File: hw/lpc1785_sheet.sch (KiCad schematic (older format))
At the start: 25 parts, among them J2 ARM_JTAG_SWD_HEADER_10_PINSMD, J3 HEADER_USART_2_SMD, U4 LPC1785FBD208_551QFP50, X1 XTAL_7A-20.000MAAJ-T

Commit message: multiple bug fixes, uv terminal SDO interface
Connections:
- wire segments 181 -> 234
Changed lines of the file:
@@
 	5500 4100 5600 4100
 Wire Wire Line
-	5500 3800 5500 4300
-Wire Wire Line
-	4700 4000 5600 4000
+	5500 3800 5500 3900
+Wire Wire Line
+	5500 3900 5500 4000
+Wire Wire Line
+	5500 4000 5500 4100
+Wire Wire Line
+	5500 4100 5500 4300
+Wire Wire Line
+	4700 4000 4850 4000
+Wire Wire Line
+	4850 4000 5000 4000
+Wire Wire Line
+	5000 4000 5150 4000
+Wire Wire Line
+	5150 4000 5500 4000
+Wire Wire Line
+	5500 4000 5600 4000
 Wire Wire Line
 	5600 3900 5500 3900
@@
 $EndComp
 Wire Wire Line
-	5400 5300 5400 5550
+	5400 5300 5400 5400
+Wire Wire Line
+	5400 5400 5400 5500
+Wire Wire Line
+	5400 5500 5400 5550
 Wire Wire Line
 	5400 5300 5600 5300
@@
 	4150 4250 4150 4350
 Wire Wire Line
-	4050 4350 4350 4350
+	4050 4350 4150 4350
+Wire Wire Line
+	4150 4350 4250 4350
+Wire Wire Line
+	4250 4350 4350 4350
 Connection ~ 4250 4350
 Wire Wire Line
@@
 Connection ~ 4150 4350
 Wire Wire Line
-	3900 4750 5250 4750
+	3900 4750 4150 4750
+Wire Wire Line
+	4150 4750 5250 4750
 Wire Wire Line
 	4150 4750 4150 4650
@@
 Connection ~ 4150 4750
 Wire Wire Line
-	3900 4950 4550 4950
-Wire Wire Line
-	4350 4650 4350 10600
+	3900 4950 4250 4950
+Wire Wire Line
+	4250 4950 4550 4950
+Wire Wire Line
+	4350 4650 4350 5450
+Wire Wire Line
+	4350 5450 4350 10600
 Connection ~ 4350 5450
 Wire Wire Line
@@
 $EndComp
 Wire Wire Line
-	4050 4850 4050 5550
+	4050 4850 4050 5050
+Wire Wire Line
+	4050 5050 4050 5550
 Wire Wire Line
 	4050 4850 3900 4850
@@
 Text Label 4550 4950 0    60   ~ 0
 SWDCLK
-Wire Wire Line
-	4350 10600 5050 10600
 Wire Wire Line
 	4350 5450 3900 5450
@@
 Connection ~ 11000 3850
 Wire Wire Line
-	10850 3850 11300 3850
+	10850 3850 11000 3850
+Wire Wire Line
+	11000 3850 11150 3850
+Wire Wire Line
+	11150 3850 11300 3850
 $Comp
 L 100nF C24
@@
 $EndComp
 Wire Wire Line
-	10850 4150 11900 4150
+	10850 4150 11000 4150
+Wire Wire Line
+	11000 4150 11150 4150
+Wire Wire Line
+	11150 4150 11800 4150
+Wire Wire Line
+	11800 4150 11900 4150
 Connection ~ 11000 4150
 Connection ~ 11150 4150
@@
 	11900 4050 11800 4050
 Wire Wire Line
-	11800 4050 11800 4350
+	11800 4050 11800 4150
+Wire Wire Line
+	11800 4150 11800 4250
+Wire Wire Line
+	11800 4250 11800 4350
 Connection ~ 11800 4150
 Wire Wire Line
@@
 Connection ~ 11800 4250
 Wire Wire Line
-	11300 3750 11900 3750
+	11300 3750 11800 3750
+Wire Wire Line
+	11800 3750 11900 3750
 Wire Wire Line
 	11300 3850 11300 3750
@@
 	11900 3650 11800 3650
 Wire Wire Line
-	11800 3550 11800 3750
+	11800 3550 11800 3650
+Wire Wire Line
+	11800 3650 11800 3750
 Connection ~ 11800 3750
 Wire Wire Line
@@
 $EndComp
 Wire Wire Line
-	4400 9700 5050 9700
+	4400 9700 4550 9700
+Wire Wire Line
+	4550 9700 4700 9700
+Wire Wire Line
+	4700 9700 4850 9700
+Wire Wire Line
+	4850 9700 4950 9700
+Wire Wire Line
+	4950 9700 5050 9700
 Connection ~ 4550 9700
 Connection ~ 4700 9700
 Connection ~ 4850 9700
 Wire Wire Line
-	4950 9700 4950 10000
+	4950 9700 4950 9800
+Wire Wire Line
+	4950 9800 4950 9900
+Wire Wire Line
+	4950 9900 4950 10000
 Wire Wire Line
 	4950 9800 5050 9800
@@
 Connection ~ 4950 9900
 Wire Wire Line
-	4400 9400 5050 9400
+	4400 9400 4550 9400
+Wire Wire Line
+	4550 9400 4700 9400
+Wire Wire Line
+	4700 9400 4850 9400
+Wire Wire Line
+	4850 9400 4950 9400
+Wire Wire Line
+	4950 9400 5050 9400
 Connection ~ 4850 9400
 Connection ~ 4700 9400
 Connection ~ 4550 9400
 Wire Wire Line
-	4950 9100 4950 9400
+	4950 9100 4950 9200
+Wire Wire Line
+	4950 9200 4950 9300
+Wire Wire Line
+	4950 9300 4950 9400
 Connection ~ 4950 9400
 Wire Wire Line
@@
 $EndComp
 Wire Wire Line
-	10750 8900 11800 8900
+	10750 8900 10900 8900
+Wire Wire Line
+	10900 8900 11050 8900
+Wire Wire Line
+	11050 8900 11700 8900
+Wire Wire Line
+	11700 8900 11800 8900
 Connection ~ 10900 8900
 Connection ~ 11050 8900
 Wire Wire Line
-	11700 8900 11700 9100
+	11700 8900 11700 9000
+Wire Wire Line
+	11700 9000 11700 9100
 Wire Wire Line
 	11700 9000 11800 9000
@@
 	10750 9250 10750 9200
 Wire Wire Line
-	10750 9200 11050 9200
+	10750 9200 10900 9200
+Wire Wire Line
+	10900 9200 11050 9200
 Connection ~ 10900 9200
 $Comp
@@
 $EndComp
 Wire Wire Line
-	11500 9500 11750 9500
+	11500 9500 11600 9500
+Wire Wire Line
+	11600 9500 11750 9500
 Wire Wire Line
 	11750 9500 11750 9400
@@
 	11750 9300 11750 9200
 Wire Wire Line
-	11750 9200 11500 9200
+	11750 9200 11600 9200
+Wire Wire Line
+	11600 9200 11500 9200
 $Comp
 L 18pF C30
@@
 Connection ~ 11600 9200
 Wire Wire Line
-	11200 9200 11200 9500
+	11200 9200 11200 9300
+Wire Wire Line
+	11200 9300 11200 9500
 $Comp
 L GND #PWR034
@@
 	11800 9600 11700 9600
 Wire Wire Line
-	11700 9600 11700 9850
+	11700 9600 11700 9700
+Wire Wire Line
+	11700 9700 11700 9800
+Wire Wire Line
+	11700 9800 11700 9850
 Wire Wire Line
 	11700 9700 11800 9700
@@
 	15800 9000 15900 9000
 Wire Wire Line
-	15800 10400 18450 10400
+	15800 10400 17000 10400
+Wire Wire Line
+	17000 10400 18350 10400
+Wire Wire Line
+	18350 10400 18450 10400
 Wire Wire Line
 	15800 10600 16700 10600
@@
 	16700 10600 16700 10300
 Wire Wire Line
-	16700 10300 18450 10300
+	16700 10300 17000 10300
+Wire Wire Line
+	17000 10300 18350 10300
+Wire Wire Line
+	18350 10300 18450 10300
 Wire Wire Line
 	18450 10200 18350 10200
@@
 $EndComp
 Wire Wire Line
-	18250 10800 18250 11000
+	18250 10800 18250 10900
+Wire Wire Line
+	18250 10900 18250 11000
 Wire Wire Line
 	18250 10800 18450 10800
@@
 	4400 9850 4400 9700
 Wire Wire Line
-	4700 4300 5150 4300
+	4700 4300 4850 4300
+Wire Wire Line
+	4850 4300 5000 4300
+Wire Wire Line
+	5000 4300 5150 4300
 Wire Wire Line
 	15900 11200 15800 11200
@@
 Wire Wire Line
 	9450 4000 8700 4000
+Wire Wire Line
+	4350 10600 5050 10600
 $EndSCHEMATC

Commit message: starting to design hw 5.0, with variable current source for LCD backlight
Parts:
- removed D4: WL-SMCW-150060BS75000-B, wurth_LEDS:Wuerth_Elektronik_LEDs_rev15b-0603, symbol WL-SMCW-150060BS75000-B
- removed J3: HEADER_USART_2_SMD, usevolt:HEADER_4_2_SMD, symbol HEADER_USART_2_SMD
- removed R8: 470, multicomp:Multicomp-RESC1608X60N, symbol 470
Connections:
- net labels removed: RXD, TXD
- wire segments 234 -> 162

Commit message: still implementing treeview, not ready
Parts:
- added R301: 10K, multicomp:0603, symbol 10K
- U4: symbol LPC1785FBD208_551QFP50 -> LPC1785FBD208_551QFP50-RESCUE-display
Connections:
- net labels removed: VDD_SENSE
- wire segments 162 -> 163
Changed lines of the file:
@@
 $EndDescr
 $Comp
-L LPC1785FBD208_551QFP50 U4
+L LPC1785FBD208_551QFP50-RESCUE-display U4
 U 1 1 57B485E7
 P 6700 5400
+AR Path="/57B485E7" Ref="U4"  Part="1"
+AR Path="/57B4853E/57B485E7" Ref="U4"  Part="1"
 F 0 "U4" H 7150 7354 45  0000 C CNN
 F 1 "LPC1785FBD208_551QFP50" H 7150 7270 45  0000 C CNN
@@
 $EndComp
 $Comp
-L LPC1785FBD208_551QFP50 U4
+L LPC1785FBD208_551QFP50-RESCUE-display U4
 U 2 1 57B48643
 P 13000 5050
+AR Path="/57B48643" Ref="U4"  Part="2"
+AR Path="/57B4853E/57B48643" Ref="U4"  Part="2"
 F 0 "U4" H 14150 6804 45  0000 C CNN
 F 1 "LPC1785FBD208_551QFP50" H 14150 6720 45  0000 C CNN
@@
 $EndComp
 $Comp
-L LPC1785FBD208_551QFP50 U4
+L LPC1785FBD208_551QFP50-RESCUE-display U4
 U 3 1 57B486B3
 P 5950 10500
+AR Path="/57B486B3" Ref="U4"  Part="3"
+AR Path="/57B4853E/57B486B3" Ref="U4"  Part="3"
 F 0 "U4" H 7050 12154 45  0000 C CNN
 F 1 "LPC1785FBD208_551QFP50" H 7050 12070 45  0000 C CNN
@@
 $EndComp
 $Comp
-L LPC1785FBD208_551QFP50 U4
+L LPC1785FBD208_551QFP50-RESCUE-display U4
 U 4 1 57B4870D
 P 12800 10600
+AR Path="/57B4870D" Ref="U4"  Part="4"
+AR Path="/57B4853E/57B4870D" Ref="U4"  Part="4"
 F 0 "U4" H 13800 12554 45  0000 C CNN
 F 1 "LPC1785FBD208_551QFP50" H 13800 12470 45  0000 C CNN
@@
 Wire Wire Line
 	9150 9100 9050 9100
-Text HLabel 9150 9800 2    60   Input ~ 0
+Text HLabel 10000 9800 2    60   Input ~ 0
 LCD_DE
 Text HLabel 9150 9900 2    60   Input ~ 0
@@
 	9050 9900 9150 9900
 Wire Wire Line
-	9150 9800 9050 9800
+	9050 9800 10000 9800
 Text HLabel 9150 10800 2    60   Input ~ 0
 EMC_A7
@@
 Connection ~ 11700 9000
 $Comp
-L GND #PWR309
+L GND #PWR310
 U 1 1 57B6EDB0
 P 10750 9250
-F 0 "#PWR309" H 10750 9000 50  0001 C CNN
+F 0 "#PWR310" H 10750 9000 50  0001 C CNN
 F 1 "GND" H 10755 9077 50  0000 C CNN
 F 2 "" H 10750 9250 50  0000 C CNN
@@
 	11800 9300 11750 9300
 Wire Wire Line
-	11750 9300 11750 9200
-Wire Wire Line
-	11750 9200 11500 9200
+	11750 9200 11750 9300
+Wire Wire Line
+	11500 9200 11750 9200
 $Comp
 L 18pF C30
@@
 	11200 9200 11200 9500
 $Comp
-L GND #PWR312
+L GND #PWR313
 U 1 1 57B6F87A
 P 11100 9400
-F 0 "#PWR312" H 11100 9150 50  0001 C CNN
+F 0 "#PWR313" H 11100 9150 50  0001 C CNN
 F 1 "GND" H 11105 9227 50  0000 C CNN
 F 2 "" H 11100 9400 50  0000 C CNN
@@
 Connection ~ 11700 9700
 $Comp
-L GND #PWR313
+L GND #PWR314
 U 1 1 57B7073F
 P 11700 9850
-F 0 "#PWR313" H 11700 9600 50  0001 C CNN
+F 0 "#PWR314" H 11700 9600 50  0001 C CNN
 F 1 "GND" H 11705 9677 50  0000 C CNN
 F 2 "" H 11700 9850 50  0000 C CNN
@@
 Wire Wire Line
 	11700 10400 11800 10400
-Text HLabel 11700 10700 0    60   Input ~ 0
+Text HLabel 5500 7300 0    60   Input ~ 0
 LCD_BACKLIGHT
 Wire Wire Line
-	11700 10700 11800 10700
-Text HLabel 15900 11200 2    60   Input ~ 0
+	5500 7300 5600 7300
+Text HLabel 5500 7200 0    60   Input ~ 0
 BUZZER
 Text HLabel 15900 12100 2    60   Input ~ 0
@@
 Wire Wire Line
 	8700 5300 8800 5300
-Wire Wire Line
-	8800 5100 8700 5100
-Text HLabel 8800 5100 2    60   Input ~ 0
-VDD_SENSE
 $Bitmap
 Pos 22650 15250
@@
 SPI_RESET
 $Comp
-L +3V3 #PWR308
+L +3V3 #PWR309
 U 1 1 57BCA081
 P 10750 8800
-F 0 "#PWR308" H 10750 8650 50  0001 C CNN
+F 0 "#PWR309" H 10750 8650 50  0001 C CNN
 F 1 "+3V3" H 10765 8973 50  0000 C CNN
 F 2 "" H 10750 8800 50  0000 C CNN
@@
 	4400 9250 4400 9400
 $Comp
-L +3V3 #PWR310
+L +3V3 #PWR311
 U 1 1 57BCB2A0
 P 10850 3700
-F 0 "#PWR310" H 10850 3550 50  0001 C CNN
+F 0 "#PWR311" H 10850 3550 50  0001 C CNN
 F 1 "+3V3" H 10865 3873 50  0000 C CNN
 F 2 "" H 10850 3700 50  0000 C CNN
@@
 	10850 3700 10850 3850
 $Comp
-L GND #PWR311
+L GND #PWR312
 U 1 1 57BCB9E7
 P 10850 4300
-F 0 "#PWR311" H 10850 4050 50  0001 C CNN
+F 0 "#PWR312" H 10850 4050 50  0001 C CNN
 F 1 "GND" H 10855 4127 50  0000 C CNN
 F 2 "" H 10850 4300 50  0000 C CNN
@@
 	4700 4300 5150 4300
 Wire Wire Line
-	15900 11200 15800 11200
+	5500 7200 5600 7200
 Wire Wire Line
 	4350 10600 5050 10600
+$Comp
+L 10K R301
+U 1 1 58F5514D
+P 9800 9950
+F 0 "R301" V 9808 10008 45  0000 L CNN
+F 1 "10K" V 9892 10008 45  0000 L CNN
+F 2 "multicomp:0603" H 9830 10100 20  0001 C CNN
+F 3 "http://www.farnell.com/datasheets/1788326.pdf?_ga=1.214208087.1948984246.1460023966" H 9769 9989 60  0001 C CNN
+F 4 "9330399" H 10169 10389 60  0001 C CNN "1st Source Part Number"
+F 5 "Farnell" H 10069 10289 60  0001 C CNN "1st Source"
+F 6 "MC0063W0603110K" H 9969 10189 60  0001 C CNN "Manufacturer Part Number"
+F 7 "MULTICOMP" H 9869 10089 60  0001 C CNN "Manufacturer"
+	1    9800 9950
+	0    1    1    0
+$EndComp
+$Comp
+L GND #PWR308
+U 1 1 58F551E0
+P 9800 10200
+F 0 "#PWR308" H 9800 9950 50  0001 C CNN
+F 1 "GND" H 9805 10027 50  0000 C CNN
+F 2 "" H 9800 10200 50  0000 C CNN
+F 3 "" H 9800 10200 50  0000 C CNN
+	1    9800 10200
+	1    0    0    -1
+$EndComp
+Wire Wire Line
+	9800 10200 9800 10150
+Wire Wire Line
+	9800 9850 9800 9800
+Connection ~ 9800 9800
 $EndSCHEMATC

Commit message: version control bug: pwr_supply_sheet now has fuse for LCD as in hw 1.5.0
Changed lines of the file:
@@
 	11800 9300 11750 9300
 Wire Wire Line
-	11750 9200 11750 9300
+	11750 9300 11750 9200
 Wire Wire Line
-	11500 9200 11750 9200
+	11750 9200 11500 9200
 $Comp
 L 18pF C30

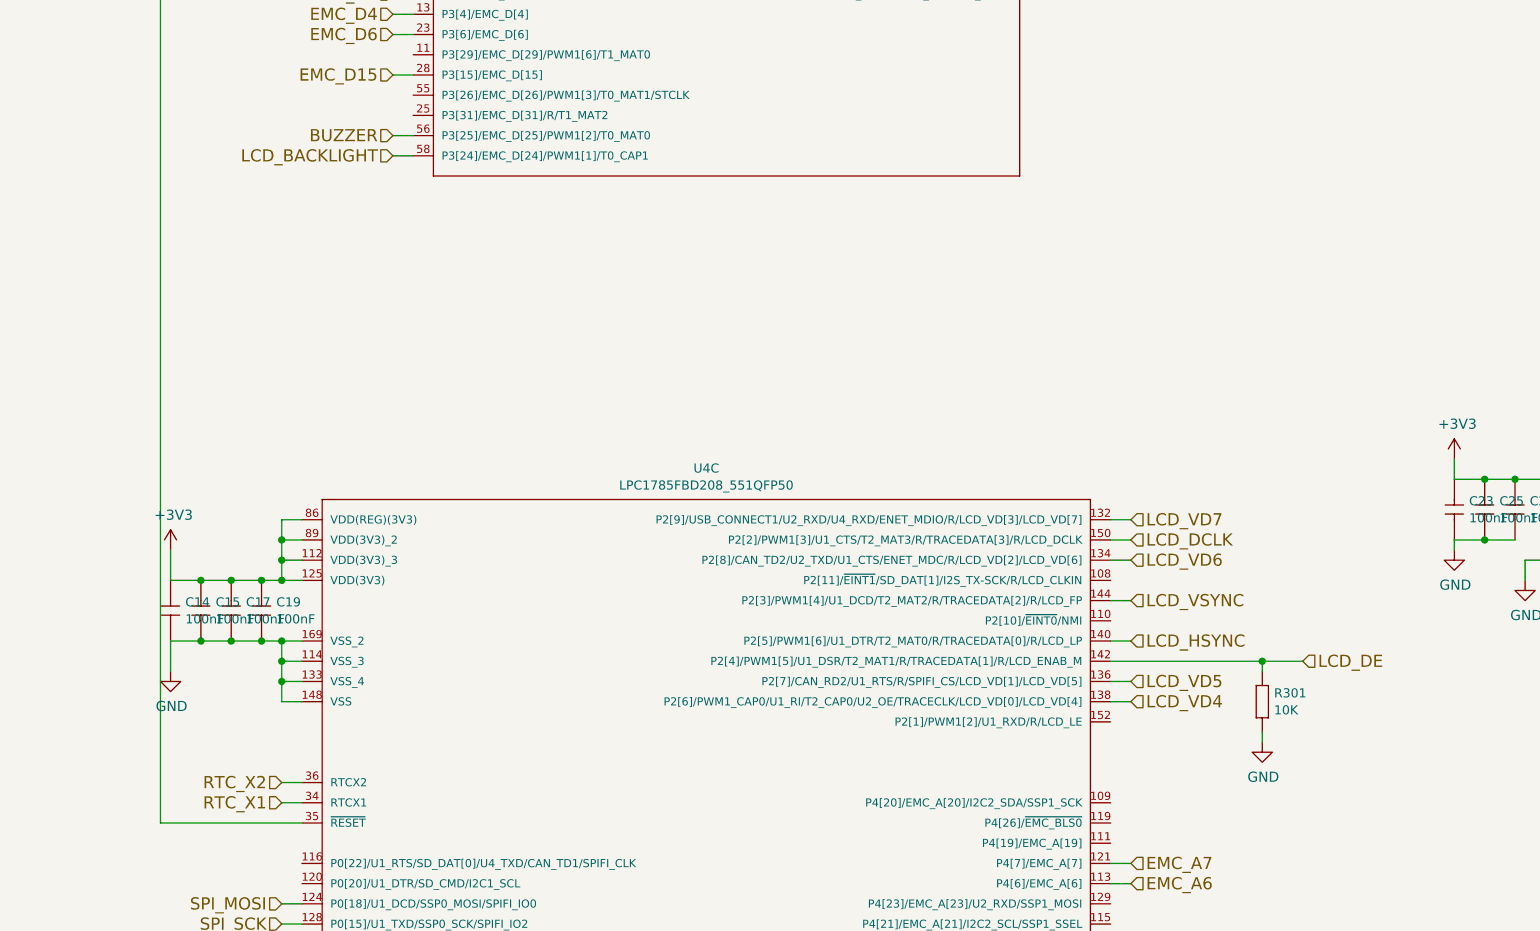
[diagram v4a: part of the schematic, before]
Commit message: hw version 1.6.0
* LCD backlight remains off while booting
* BUZZER amplifying MOSFET circuit changed to low side driving
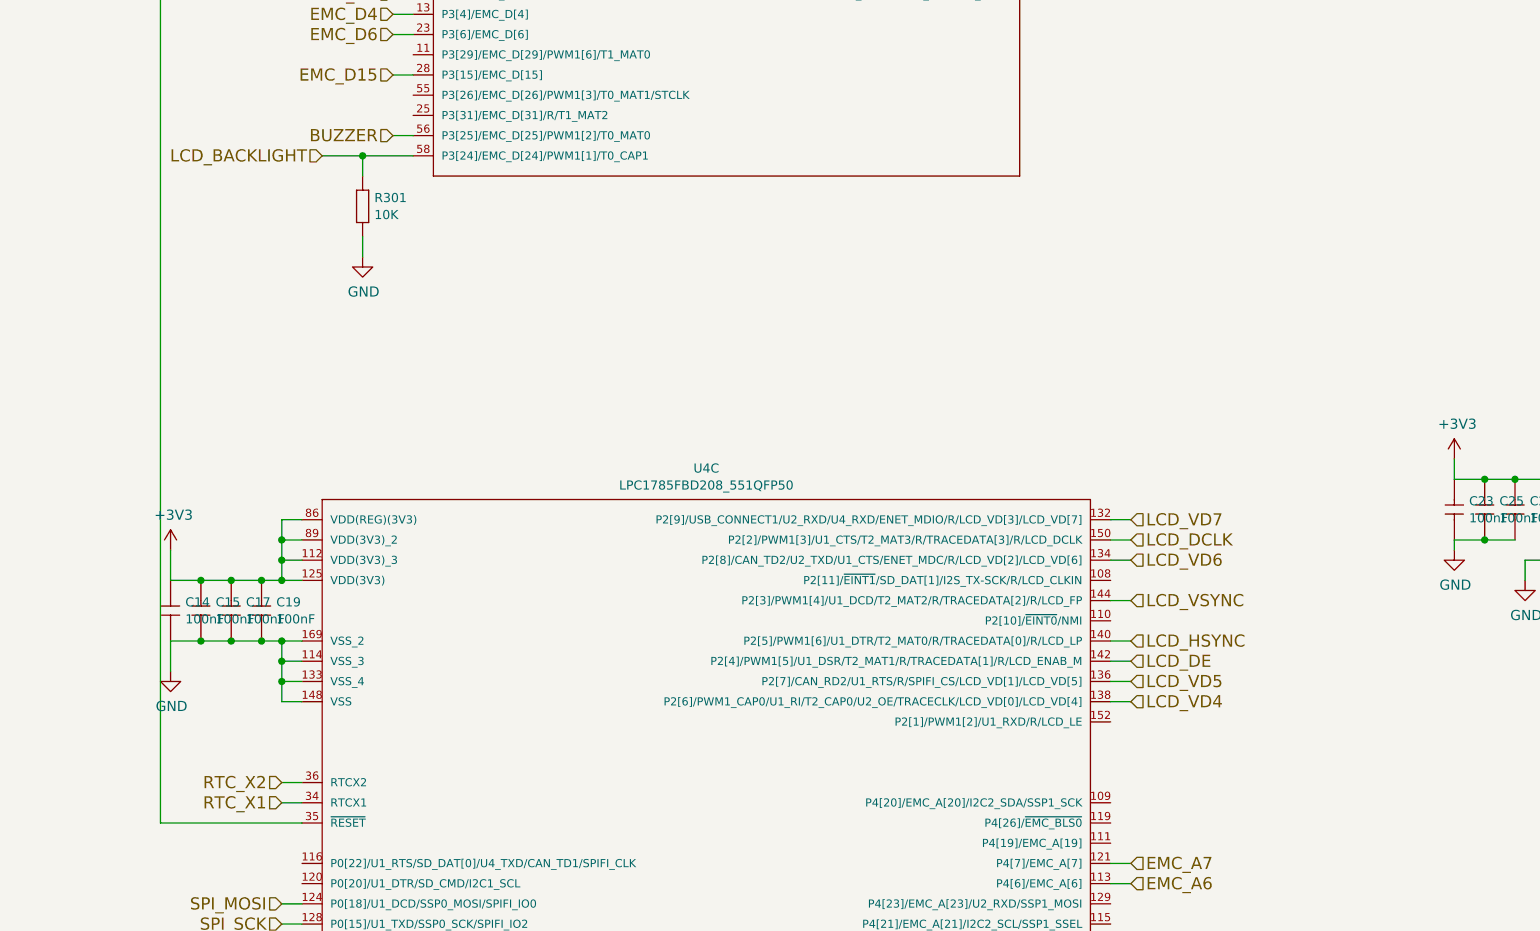
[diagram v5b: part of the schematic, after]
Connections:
- net LCD_BACKLIGHT: now also R301.2 (R2)
- net LCD_DE: no longer R301.2 (R2)
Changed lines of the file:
@@
 	4700 4400 4700 4300
 $Comp
-L GND #PWR307
+L GND #PWR308
 U 1 1 57B55D95
 P 5400 5550
-F 0 "#PWR307" H 5400 5300 50  0001 C CNN
+F 0 "#PWR308" H 5400 5300 50  0001 C CNN
 F 1 "GND" H 5405 5377 50  0000 C CNN
 F 2 "" H 5400 5550 50  0000 C CNN
@@
 Wire Wire Line
 	9150 9100 9050 9100
-Text HLabel 10000 9800 2    60   Input ~ 0
+Text HLabel 9150 9800 2    60   Input ~ 0
 LCD_DE
 Text HLabel 9150 9900 2    60   Input ~ 0
@@
 	9050 9900 9150 9900
 Wire Wire Line
-	9050 9800 10000 9800
+	9050 9800 9150 9800
 Text HLabel 9150 10800 2    60   Input ~ 0
 EMC_A7
@@
 Wire Wire Line
 	11700 10400 11800 10400
-Text HLabel 5500 7300 0    60   Input ~ 0
+Text HLabel 5150 7300 0    60   Input ~ 0
 LCD_BACKLIGHT
 Wire Wire Line
-	5500 7300 5600 7300
+	5150 7300 5600 7300
 Text HLabel 5500 7200 0    60   Input ~ 0
 BUZZER
@@
 Wire Wire Line
 	4350 10600 5050 10600
+Wire Wire Line
+	5350 7400 5350 7300
+Connection ~ 5350 7300
+$Comp
+L GND #PWR307
+U 1 1 59507EAE
+P 5350 7800
+F 0 "#PWR307" H 5350 7550 50  0001 C CNN
+F 1 "GND" H 5355 7627 50  0000 C CNN
+F 2 "" H 5350 7800 50  0000 C CNN
+F 3 "" H 5350 7800 50  0000 C CNN
+	1    5350 7800
+	1    0    0    -1
+$EndComp
+Wire Wire Line
+	5350 7800 5350 7700
 $Comp
 L 10K R301
-U 1 1 58F5514D
-P 9800 9950
-F 0 "R301" V 9808 10008 45  0000 L CNN
-F 1 "10K" V 9892 10008 45  0000 L CNN
-F 2 "multicomp:0603" H 9830 10100 20  0001 C CNN
-F 3 "http://www.farnell.com/datasheets/1788326.pdf?_ga=1.214208087.1948984246.1460023966" H 9769 9989 60  0001 C CNN
-F 4 "9330399" H 10169 10389 60  0001 C CNN "1st Source Part Number"
-F 5 "Farnell" H 10069 10289 60  0001 C CNN "1st Source"
-F 6 "MC0063W0603110K" H 9969 10189 60  0001 C CNN "Manufacturer Part Number"
-F 7 "MULTICOMP" H 9869 10089 60  0001 C CNN "Manufacturer"
-	1    9800 9950
-	0    1    1    0
-$EndComp
-$Comp
-L GND #PWR308
-U 1 1 58F551E0
-P 9800 10200
-F 0 "#PWR308" H 9800 9950 50  0001 C CNN
-F 1 "GND" H 9805 10027 50  0000 C CNN
-F 2 "" H 9800 10200 50  0000 C CNN
-F 3 "" H 9800 10200 50  0000 C CNN
-	1    9800 10200
-	1    0    0    -1
-$EndComp
-Wire Wire Line
-	9800 10200 9800 10150
-Wire Wire Line
-	9800 9850 9800 9800
-Connection ~ 9800 9800
+U 1 1 595084C8
+P 5350 7500
+F 0 "R301" V 5358 7558 45  0000 L CNN
+F 1 "10K" V 5442 7558 45  0000 L CNN
+F 2 "multicomp:0603" H 5380 7650 20  0001 C CNN
+F 3 "http://www.farnell.com/datasheets/1788326.pdf?_ga=1.214208087.1948984246.1460023966" H 5319 7539 60  0001 C CNN
+F 4 "9330399" H 5719 7939 60  0001 C CNN "1st Source Part Number"
+F 5 "Farnell" H 5619 7839 60  0001 C CNN "1st Source"
+F 6 "MC0063W0603110K" H 5519 7739 60  0001 C CNN "Manufacturer Part Number"
+F 7 "MULTICOMP" H 5419 7639 60  0001 C CNN "Manufacturer"
+	1    5350 7500
+	0    1    1    0
+$EndComp
 $EndSCHEMATC

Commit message: small modifications to schematic
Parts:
- removed R301: 10K, multicomp:0603, symbol 10K
- added R?: 1K, multicomp:0603, symbol 1K
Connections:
- net GND: now also R?.1 (R1)
- net LCD_BACKLIGHT: now also R?.2 (R2)
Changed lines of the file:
@@
 	5350 7800 5350 7700
 $Comp
-L 10K R301
-U 1 1 595084C8
+L 1K R?
+U 1 1 59515664
 P 5350 7500
-F 0 "R301" V 5358 7558 45  0000 L CNN
-F 1 "10K" V 5442 7558 45  0000 L CNN
+F 0 "R?" V 5358 7558 45  0000 L CNN
+F 1 "1K" V 5442 7558 45  0000 L CNN
 F 2 "multicomp:0603" H 5380 7650 20  0001 C CNN
-F 3 "http://www.farnell.com/datasheets/1788326.pdf?_ga=1.214208087.1948984246.1460023966" H 5319 7539 60  0001 C CNN
-F 4 "9330399" H 5719 7939 60  0001 C CNN "1st Source Part Number"
+F 3 "" H 5319 7539 60  0001 C CNN
+F 4 "9330380" H 5719 7939 60  0001 C CNN "1st Source Part Number"
 F 5 "Farnell" H 5619 7839 60  0001 C CNN "1st Source"
-F 6 "MC0063W0603110K" H 5519 7739 60  0001 C CNN "Manufacturer Part Number"
+F 6 "MC0063W060311K" H 5519 7739 60  0001 C CNN "Manufacturer Part Number"
 F 7 "MULTICOMP" H 5419 7639 60  0001 C CNN "Manufacturer"
 	1    5350 7500
